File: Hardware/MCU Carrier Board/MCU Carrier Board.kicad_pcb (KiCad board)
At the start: 2 copper layers, 30 x 50 mm, 0 parts

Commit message: update
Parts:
- added C10: 1uF, Capacitor_SMD:C_0603_1608Metric_Pad1.08x0.95mm_HandSolder, F.Cu at (210.4, 67.0)
- added C11: 1uF, Capacitor_SMD:C_0603_1608Metric_Pad1.08x0.95mm_HandSolder, F.Cu at (210.4, 69.5)
- added C12: 1uF, Capacitor_SMD:C_0603_1608Metric_Pad1.08x0.95mm_HandSolder, F.Cu at (210.4, 72.0)
- added C9: 1uF, Capacitor_SMD:C_0603_1608Metric_Pad1.08x0.95mm_HandSolder, F.Cu at (210.4, 64.5)
- added D4: LED, LED_SMD:LED_0603_1608Metric_Pad1.05x0.95mm_HandSolder, F.Cu at (213.8, 89.5)
- added D5: LED, LED_SMD:LED_0603_1608Metric_Pad1.05x0.95mm_HandSolder, F.Cu at (213.8, 92.0)
- added D6: LED, LED_SMD:LED_0603_1608Metric_Pad1.05x0.95mm_HandSolder, F.Cu at (213.8, 94.6)
- added D7: LED, LED_SMD:LED_0603_1608Metric_Pad1.05x0.95mm_HandSolder, F.Cu at (213.8, 97.2)
- added J2: Conn_01x05_Pin, Connector_JST:JST_EH_S5B-EH_1x05_P2.50mm_Horizontal, B.Cu at (143.0, 120.4)
- added J7: Top Connector, DF40C:HRS_DF40C-20DS-0.4V_51_, B.Cu at (145.9, 67.6)
- added J8: Bottom Connector, DF40C:HRS_DF40C-20DS-0.4V_51_, B.Cu at (145.9, 91.1)
- added R10: 1K, Resistor_SMD:R_0603_1608Metric_Pad0.98x0.95mm_HandSolder, F.Cu at (218.1, 96.9)
- added R7: 1K, Resistor_SMD:R_0603_1608Metric_Pad0.98x0.95mm_HandSolder, F.Cu at (218.1, 89.4)
- added R8: 1K, Resistor_SMD:R_0603_1608Metric_Pad0.98x0.95mm_HandSolder, F.Cu at (218.1, 91.9)
- added R9: 1K, Resistor_SMD:R_0603_1608Metric_Pad0.98x0.95mm_HandSolder, F.Cu at (218.1, 94.4)
- added SW1: SW_Push, Button_Switch_SMD:SW_Push_1P1T_XKB_TS-1187A, F.Cu at (145.9, 61.0)
- added SW10: SW_Push, Button_Switch_THT:SW_PUSH_6mm, F.Cu at (104.0, 44.8)
- added SW11: SW_Push, Button_Switch_THT:SW_PUSH_6mm, F.Cu at (181.0, 65.2)
- added SW12: SW_Push, Button_Switch_THT:SW_PUSH_6mm, F.Cu at (181.0, 73.8)
- added SW13: SW_Push, Button_Switch_THT:SW_PUSH_6mm, F.Cu at (181.0, 82.3)
- added SW14: SW_Push, Button_Switch_THT:SW_PUSH_6mm, F.Cu at (191.5, 65.2)
- added SW15: SW_Push, Button_Switch_THT:SW_PUSH_6mm, F.Cu at (191.5, 73.8)
- added SW16: SW_Push, Button_Switch_THT:SW_PUSH_6mm, F.Cu at (191.5, 82.3)
- added SW2: SW_Push, Button_Switch_SMD:SW_Push_1P1T_XKB_TS-1187A, F.Cu at (135.1, 79.7)
- added SW3: SW_Push, Button_Switch_SMD:SW_Push_1P1T_XKB_TS-1187A, F.Cu at (156.6, 79.7)
- added SW5: SW_Push, Button_Switch_THT:SW_PUSH_6mm, F.Cu at (123.0, 93.6)
- added SW6: SW_Push, Button_Switch_THT:SW_PUSH_6mm, F.Cu at (122.8, 110.7)
- added SW7: SW_Push, Button_Switch_THT:SW_PUSH_6mm, F.Cu at (113.1, 102.0)
- added SW8: SW_Push, Button_Switch_THT:SW_PUSH_6mm, F.Cu at (131.9, 102.5)
- added SW9: SW_Push, Button_Switch_THT:SW_PUSH_6mm, F.Cu at (102.1, 33.6)
- added U3: Left Joystick, COM_09032:XDCR_COM-09032, F.Cu at (106.9, 80.2)
- added U4: Right Joystick, COM_09032:XDCR_COM-09032, F.Cu at (166.0, 102.9)
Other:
- board outline removed

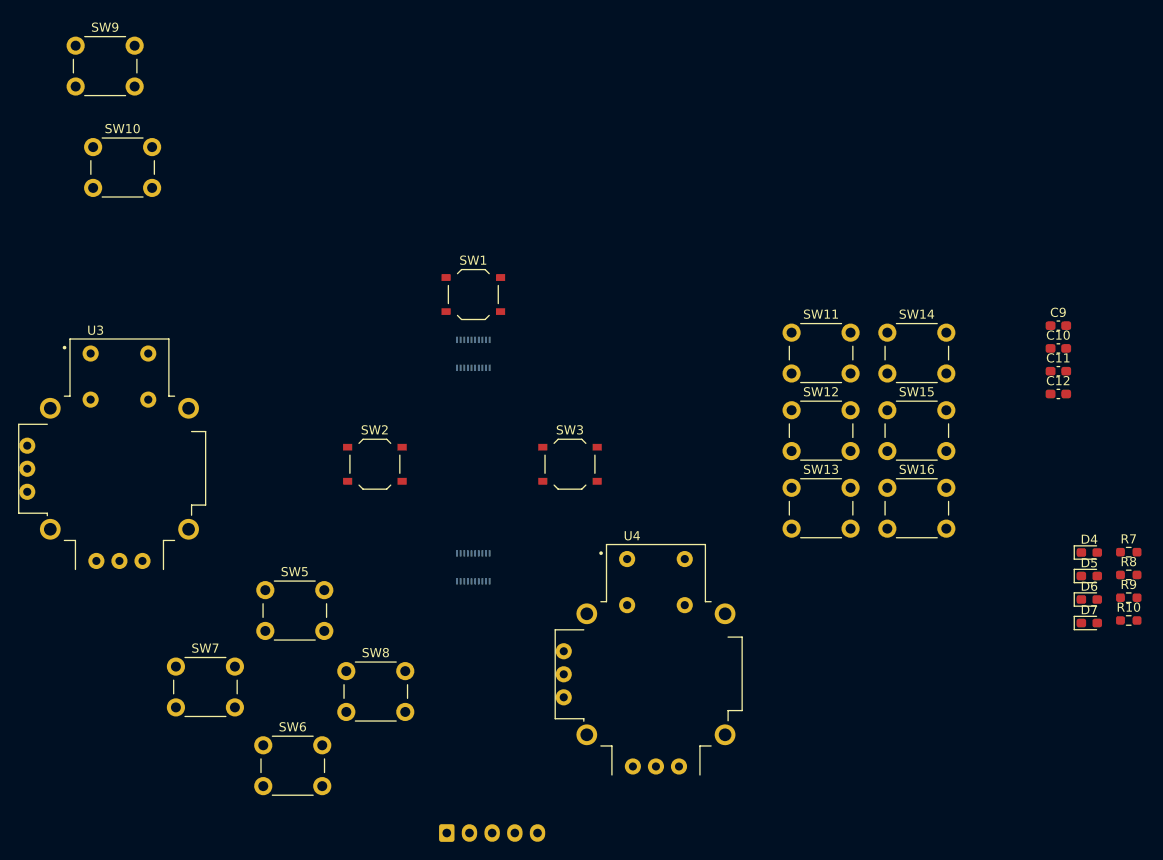
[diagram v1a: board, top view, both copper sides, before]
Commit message: locked placement of key components
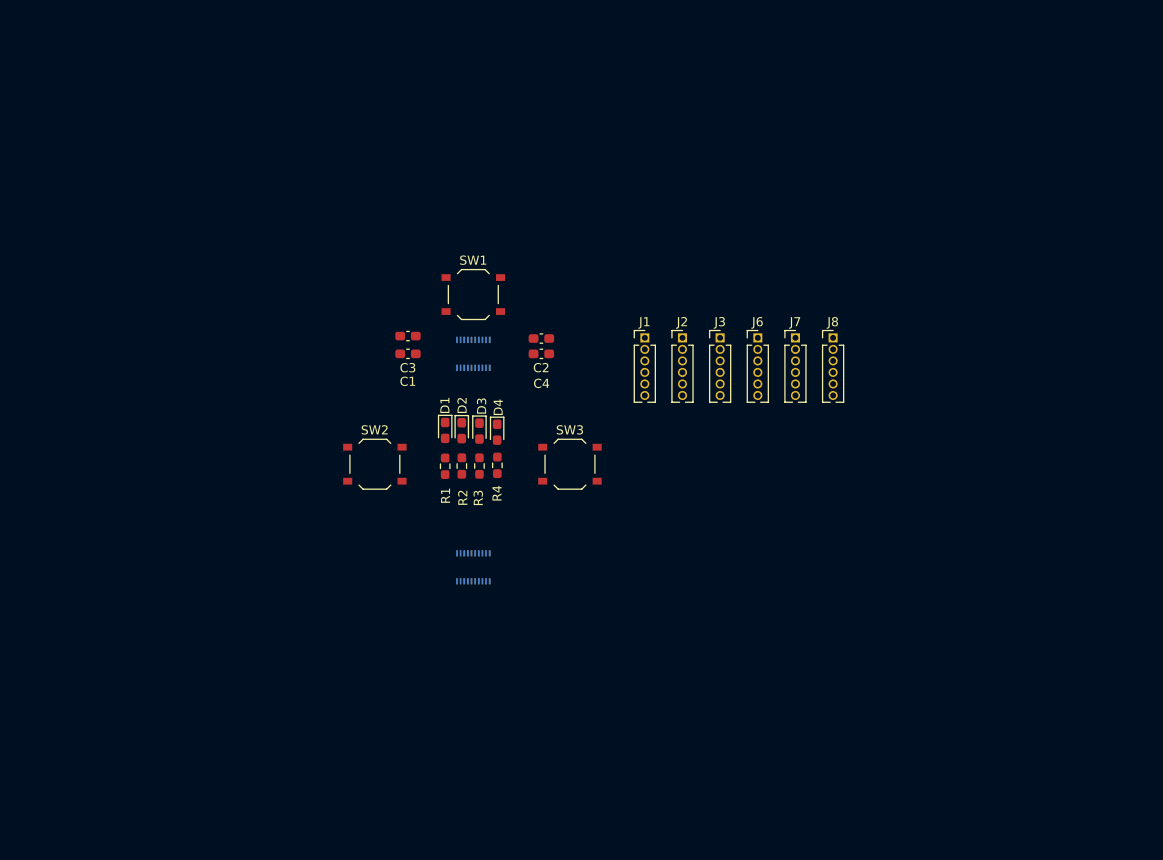
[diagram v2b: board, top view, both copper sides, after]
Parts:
- removed C10, C11, C12, C9: 1uF, Capacitor_SMD:C_0603_1608Metric_Pad1.08x0.95mm_HandSolder
- removed SW10, SW11, SW12, SW13, SW14, SW15, SW16, SW5, SW6, SW7, SW8, SW9: SW_Push, Button_Switch_THT:SW_PUSH_6mm
- removed U3: Left Joystick, COM_09032:XDCR_COM-09032
- removed U4: Right Joystick, COM_09032:XDCR_COM-09032
- added C1: .1uF, Capacitor_SMD:C_0603_1608Metric_Pad1.08x0.95mm_HandSolder, F.Cu at (138.7, 67.6)
- added C2: .1uF, Capacitor_SMD:C_0603_1608Metric_Pad1.08x0.95mm_HandSolder, F.Cu at (153.4, 65.9)
- added C3: 10uF, Capacitor_SMD:C_0603_1608Metric_Pad1.08x0.95mm_HandSolder, F.Cu at (138.7, 65.6)
- added C4: 10uF, Capacitor_SMD:C_0603_1608Metric_Pad1.08x0.95mm_HandSolder, F.Cu at (153.4, 67.6)
- added J1: Conn_01x06_Pin, Connector_PinHeader_1.27mm:PinHeader_1x06_P1.27mm_Vertical, F.Cu at (164.8, 65.8)
- added J3: Conn_01x06_Pin, Connector_PinHeader_1.27mm:PinHeader_1x06_P1.27mm_Vertical, F.Cu at (173.1, 65.8)
- added J6: Conn_01x06_Pin, Connector_PinHeader_1.27mm:PinHeader_1x06_P1.27mm_Vertical, F.Cu at (177.2, 65.8)
- added J7: Conn_01x06_Pin, Connector_PinHeader_1.27mm:PinHeader_1x06_P1.27mm_Vertical, F.Cu at (181.4, 65.8)
- added J8: Conn_01x06_Pin, Connector_PinHeader_1.27mm:PinHeader_1x06_P1.27mm_Vertical, F.Cu at (185.6, 65.8)
- J2: value Conn_01x05_Pin -> Conn_01x06_Pin; footprint Connector_JST:JST_EH_S5B-EH_1x05_P2.50mm_Horizontal -> Connector_PinHeader_1.27mm:PinHeader_1x06_P1.27mm_Vertical; moved to F.Cu
- moved R1 75.9 mm to (142.8, 80.0), turned to 90 degrees
- moved R2 74.5 mm to (144.6, 79.9), turned to 90 degrees
- moved R3 73.0 mm to (146.6, 79.9), turned to 90 degrees
- moved D1 72.2 mm to (142.8, 76.0), turned to -90 degrees
- moved R4 71.6 mm to (148.6, 79.8), turned to 90 degrees
- moved D2 71.0 mm to (144.6, 76.0), turned to -90 degrees
- moved D3 69.7 mm to (146.6, 76.1), turned to -90 degrees
- moved D4 68.6 mm to (148.5, 76.2), turned to -90 degrees
- moved J2 60.4 mm to (168.9, 65.8)
- renumbered D4 to D1, D5 to D2, D6 to D3, D7 to D4, J7 to J4, J8 to J5, R7 to R1, R8 to R2, R9 to R3, R10 to R4
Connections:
- J2 pad 1: TXD0 -> VCC_3V3
- J2 pad 2: RXD0 -> GPIO4
- J2 pad 3: GND -> GPIO5
- J2 pad 4: GPIO42 -> GPIO16
- J2 pad 5: GPIO41 -> unconnected-(J2-Pin_5-Pad5)

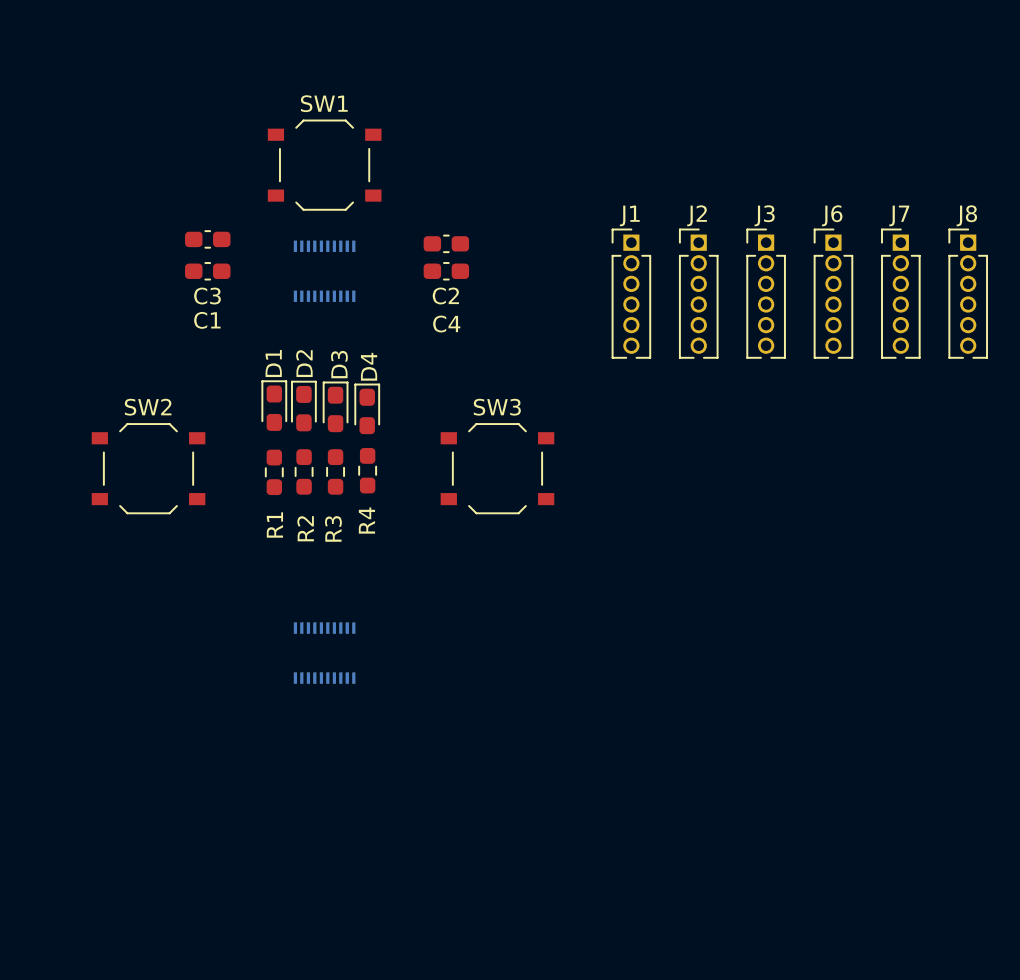
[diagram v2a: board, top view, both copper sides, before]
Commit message: reconfigured pins and started routing
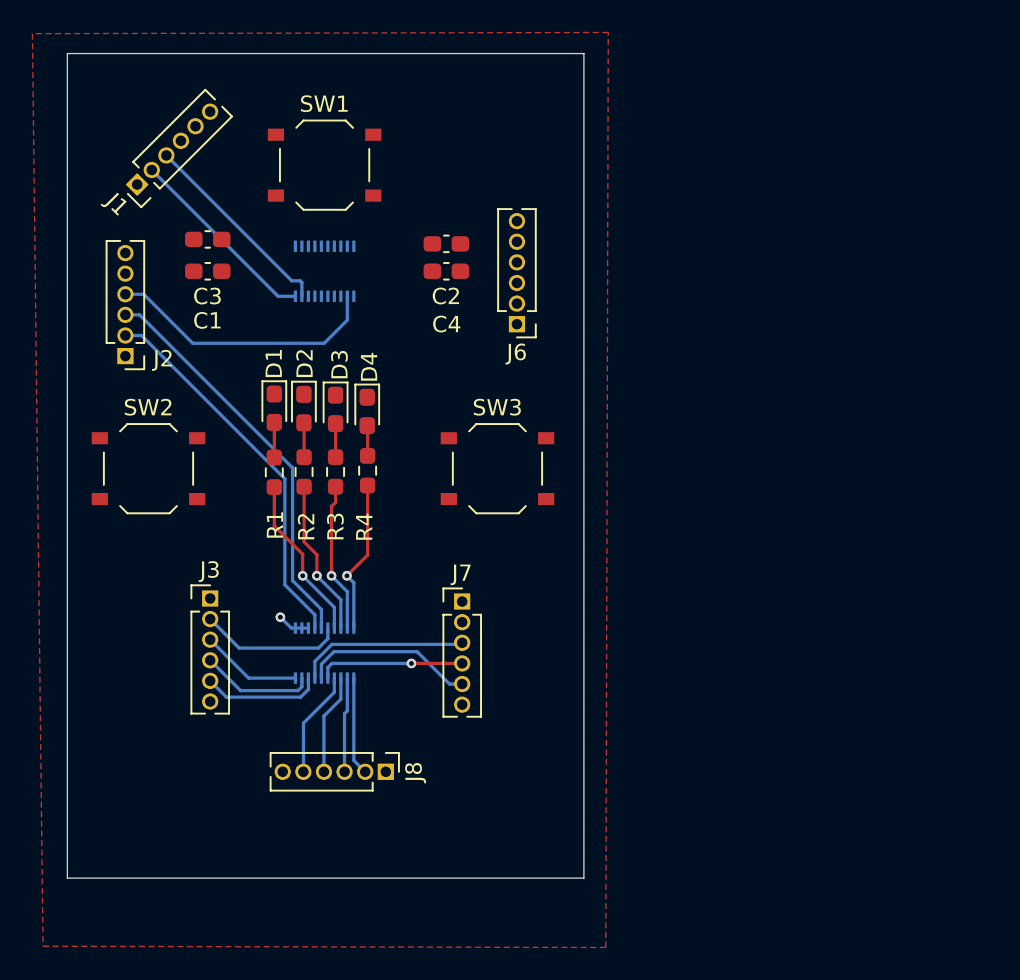
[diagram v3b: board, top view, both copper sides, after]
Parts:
- moved J8 48.5 mm to (149.7, 98.4), turned to -90 degrees
- moved J3 40.7 mm to (138.8, 87.7)
- moved J2 36.0 mm to (133.6, 72.8), turned to 180 degrees
- moved J7 34.9 mm to (154.4, 87.9)
- moved J1 30.7 mm to (134.4, 62.2), turned to 135 degrees
- moved J6 20.1 mm to (157.8, 70.8), turned to 180 degrees
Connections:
- J1 pad 3: GPIO6 -> GPIO8
- J1 pad 5: GPIO17 -> GPIO9
- J2 pad 2: GPIO4 -> GPIO17
- J2 pad 3: GPIO5 -> GPIO16
- J2 pad 4: GPIO16 -> GPIO14
- J3 pad 2: GPIO11 -> GPIO15
- J3 pad 3: GPIO12 -> GPIO7
- J3 pad 4: GPIO13 -> GPIO6
- J3 pad 5: GPIO14 -> GPIO5
- J6 pad 3: GPIO9 -> GPIO11
- J6 pad 4: GPIO8 -> GPIO12
- J6 pad 5: GPIO7 -> GPIO13
- J7 pad 3: GPIO15 -> GPIO4
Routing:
- net GPIO16: track 0.00 -> 24.8 mm
- net GPIO17: track 0.00 -> 23.4 mm
- net GPIO14: track 0.00 -> 17.0 mm
- net GPIO8: track 0.00 -> 12.4 mm
- net GPIO18: track 0.00 -> 12.1 mm
- net GPIO1: track 0.00 -> 10.7 mm
- net GPIO4: track 0.00 -> 10.6 mm
- net GPIO38: track 0.00 -> 10.2 mm, vias 0 -> 1
- net GPIO37: track 0.00 -> 9.65 mm, vias 0 -> 1
- net GPIO35: track 0.00 -> 9.49 mm, vias 0 -> 1
- net GPIO36: track 0.00 -> 9.22 mm, vias 0 -> 1
- net GPIO2: track 0.00 -> 9.03 mm, vias 0 -> 1
- net GPIO15: track 0.00 -> 8.88 mm
- net GPIO5: track 0.00 -> 7.36 mm
- net GPIO6: track 0.00 -> 7.06 mm
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- added copper zone on F.Cu, net GND
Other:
- board outline added: 31.8 x 50.8 mm

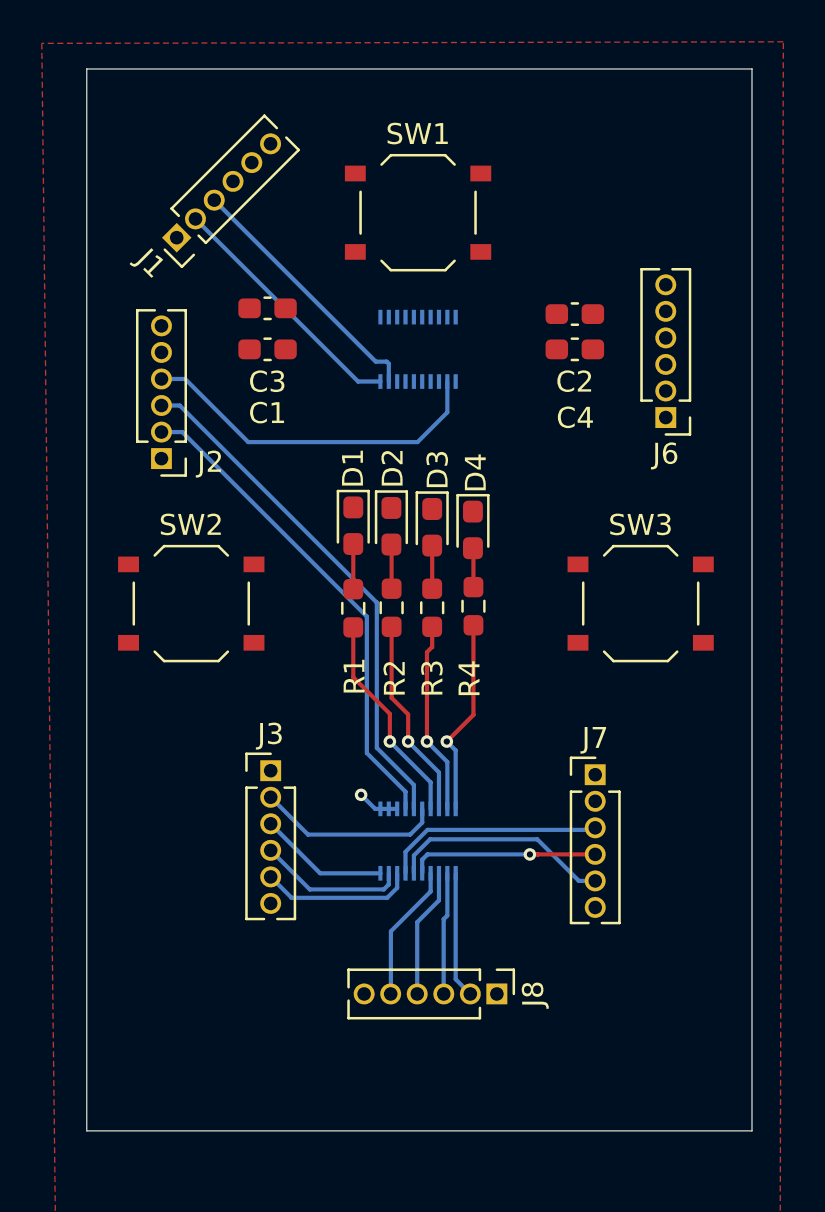
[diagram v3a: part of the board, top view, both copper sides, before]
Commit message: Added design rule made v.1 of board
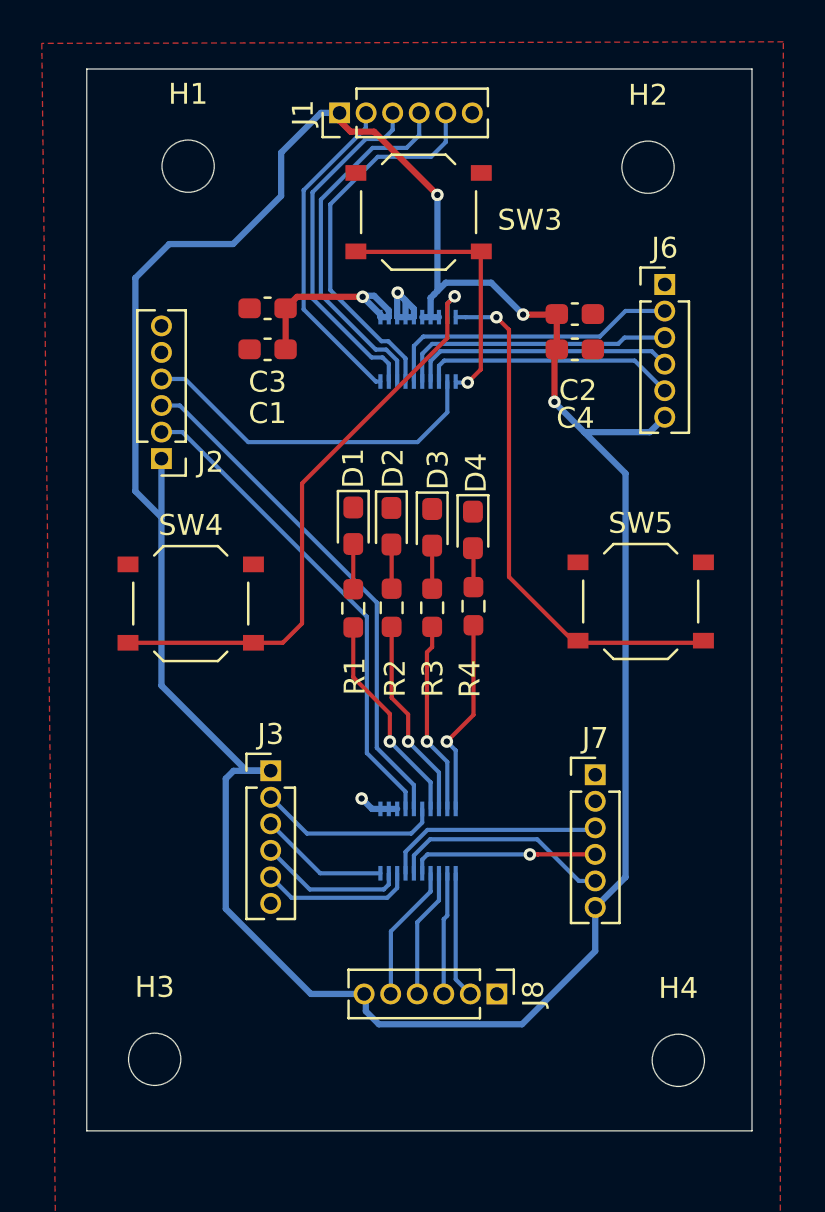
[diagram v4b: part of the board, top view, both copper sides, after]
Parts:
- removed SW1, SW2: SW_Push, Button_Switch_SMD:SW_Push_1P1T_XKB_TS-1187A
- added H1: MountingHole, MountingHole:MountingHole_2.5mm, F.Cu at (134.9, 58.8)
- added H2: MountingHole, MountingHole:MountingHole_2.5mm, F.Cu at (156.9, 58.9)
- added H3: MountingHole, MountingHole:MountingHole_2.5mm, F.Cu at (133.3, 101.5)
- added H4: MountingHole, MountingHole:MountingHole_2.5mm, F.Cu at (158.3, 101.6)
- added SW4: SW_Push, Button_Switch_SMD:SW_Push_1P1T_XKB_TS-1187A, F.Cu at (135.0, 79.7)
- added SW5: SW_Push, Button_Switch_SMD:SW_Push_1P1T_XKB_TS-1187A, F.Cu at (156.6, 79.6)
- moved SW3 21.5 mm to (145.9, 61.0)
- moved J1 9.82 mm to (142.1, 56.2), turned to 90 degrees
- moved J6 6.37 mm to (157.7, 64.5), turned to 0 degrees
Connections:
- SW3 pad 2: GPIO48 -> GPIO21
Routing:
- net VCC_3V3: track 0.00 -> 130.9 mm, vias 0 -> 3
- net GPIO47: track 0.00 -> 28.5 mm, vias 0 -> 1
- net GPIO48: track 0.00 -> 25.2 mm, vias 0 -> 1
- net GPIO9: track 0.00 -> 18.3 mm
- net GPIO3: track 0.00 -> 17.6 mm
- net GPIO10: track 0.00 -> 14.4 mm
- net GPIO11: track 0.00 -> 13.2 mm
- net GPIO21: track 0.00 -> 13.1 mm, vias 0 -> 1
- net GPIO12: track 0.00 -> 12.6 mm
- net GPIO13: track 0.00 -> 12.3 mm
- net VCC_5V: track 0.00 -> 9.49 mm, vias 0 -> 1
- net GND: track 2.00 -> 6.71 mm, vias 1 -> 2
- net GPIO8: track 12.4 -> 16.8 mm
- net GPIO18: track 12.1 -> 15.7 mm
